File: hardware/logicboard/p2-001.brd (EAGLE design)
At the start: 72 x 72 mm, 53 parts, among them IC1 5V, IC2 4066N, IC3 LTC485N, IC4 74LS07N, J1 LED, J2 PWR, J3 Display, K1 G5V1, Q1 220mA/50V/3.5Ω, Q2 220mA/50V/3.5Ω, T1 2SC1815, U1 DS18B20

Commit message: Pull-down resistor from 100 to 10k.
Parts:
- RN3: value 100 -> 10k
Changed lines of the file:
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@@
 <attribute name="VALUE" x="22" y="36" size="0.8128" layer="27" ratio="10" rot="R90" align="bottom-center"/>
 </element>
-<element name="RN3" library="resistor-net" library_urn="urn:adsk.eagle:library:343" package="RN-5" package3d_urn="urn:adsk.eagle:package:24976/1" value="100" x="24" y="42" smashed="yes" rot="R270">
+<element name="RN3" library="resistor-net" library_urn="urn:adsk.eagle:library:343" package="RN-5" package3d_urn="urn:adsk.eagle:package:24976/1" value="10k" x="24" y="42" smashed="yes" rot="R270">
 <attribute name="MF" value="" x="24" y="42" size="1.778" layer="27" rot="R270" display="off"/>
 <attribute name="MPN" value="" x="24" y="42" size="1.778" layer="27" rot="R270" display="off"/>

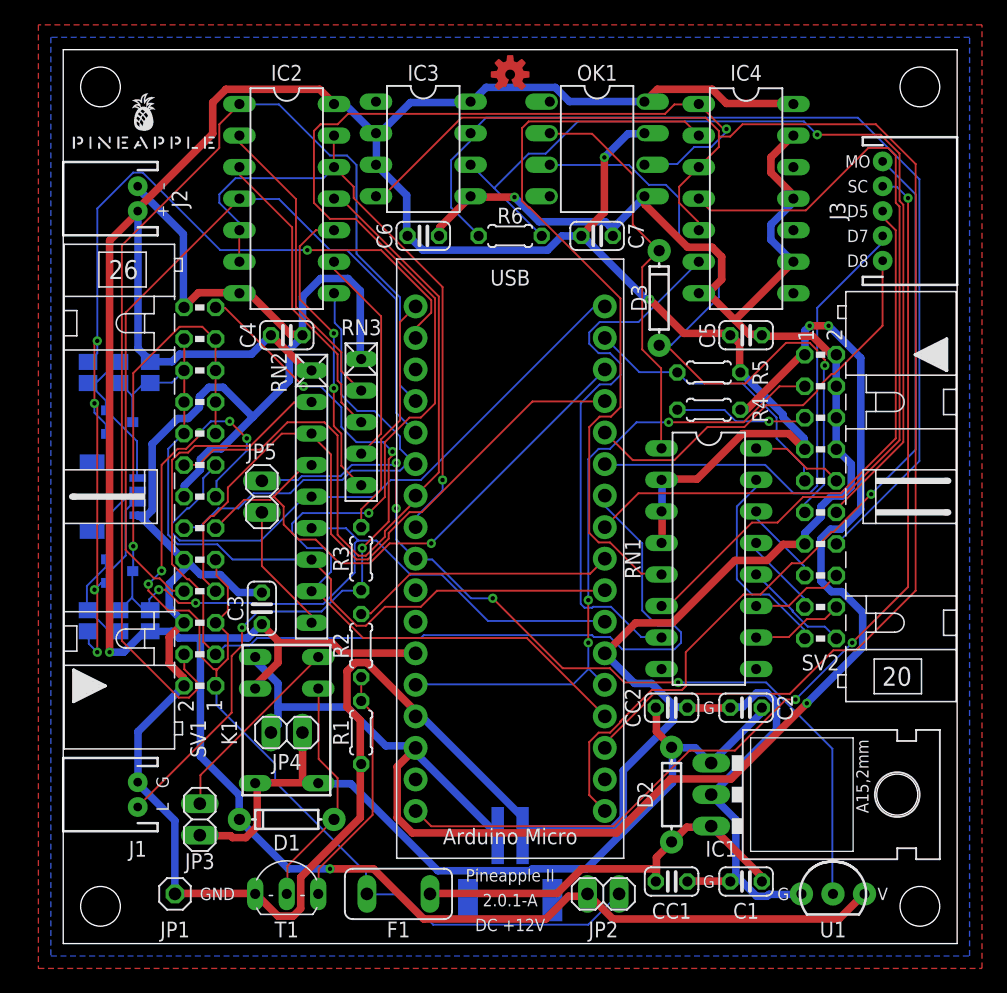
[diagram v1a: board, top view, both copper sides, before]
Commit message: Changed pinout of Display port.
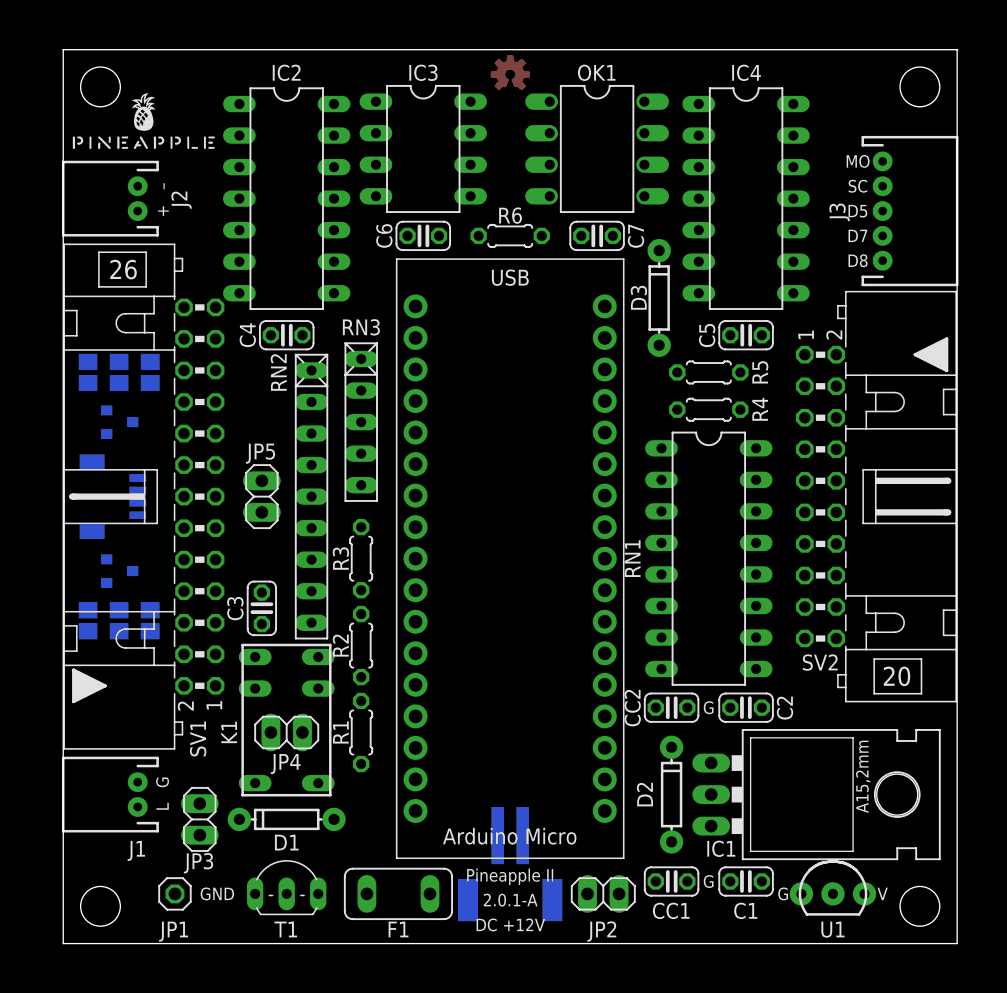
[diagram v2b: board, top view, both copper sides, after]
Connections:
- net DISP1: now also J3.1; no longer J3.3
- net DISP2: now also J3.2; no longer J3.4
- net DISP3: now also J3.3; no longer J3.5
- net MOSI: now also J3.4; no longer J3.1
- net SCLK: now also J3.5; no longer J3.2
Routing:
- net GND: track 338.6 -> 0.00 mm, vias 1 -> 0
- net VCC: track 311.7 -> 0.00 mm, vias 4 -> 0
- net RX: track 124.2 -> 0.00 mm, vias 2 -> 0
- net TX: track 123.2 -> 0.00 mm
- net +12V: track 121.4 -> 0.00 mm, vias 3 -> 0
- net +5V: track 91.2 -> 0.00 mm, vias 5 -> 0
- net ANLG1: track 91.1 -> 0.00 mm
- net VDD: track 87.9 -> 0.00 mm, vias 5 -> 0
- net SDA: track 86.4 -> 0.00 mm, vias 3 -> 0
- net DTCT1: track 84.4 -> 0.00 mm
- net SCLK: track 81.9 -> 0.00 mm, vias 3 -> 0
- net MTX-: track 80.7 -> 0.00 mm
- net MTX+: track 75.3 -> 0.00 mm, vias 1 -> 0
- net THS: track 71.5 -> 0.00 mm, vias 4 -> 0
- net V12V: track 69.7 -> 0.00 mm
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- removed copper zone on layer 1, net GND
- removed copper zone on layer 16, net GND

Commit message: Document update.
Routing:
- net GND: track 0.00 -> 325.6 mm, vias 0 -> 4
- net VCC: track 0.00 -> 306.2 mm, vias 0 -> 3
- net RX: track 0.00 -> 111.5 mm
- net +12V: track 0.00 -> 98.2 mm, vias 0 -> 1
- net LED0A: track 0.00 -> 97.9 mm, vias 0 -> 2
- net TX: track 0.00 -> 90.9 mm, vias 0 -> 2
- net ANLG1: track 0.00 -> 86.0 mm, vias 0 -> 1
- net MTX-: track 0.00 -> 81.7 mm
- net VDD: track 0.00 -> 79.1 mm, vias 0 -> 3
- net SDA: track 0.00 -> 78.2 mm, vias 0 -> 2
- net DTCT1: track 0.00 -> 75.2 mm
- net ANLG2: track 0.00 -> 73.9 mm, vias 0 -> 1
- net SCLK: track 0.00 -> 72.7 mm
- net +5V: track 0.00 -> 72.2 mm, vias 0 -> 1
- net V12V: track 0.00 -> 69.6 mm
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- added copper zone on layer 1, net GND
- added copper zone on layer 16, net GND
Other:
- board text added: "F1"

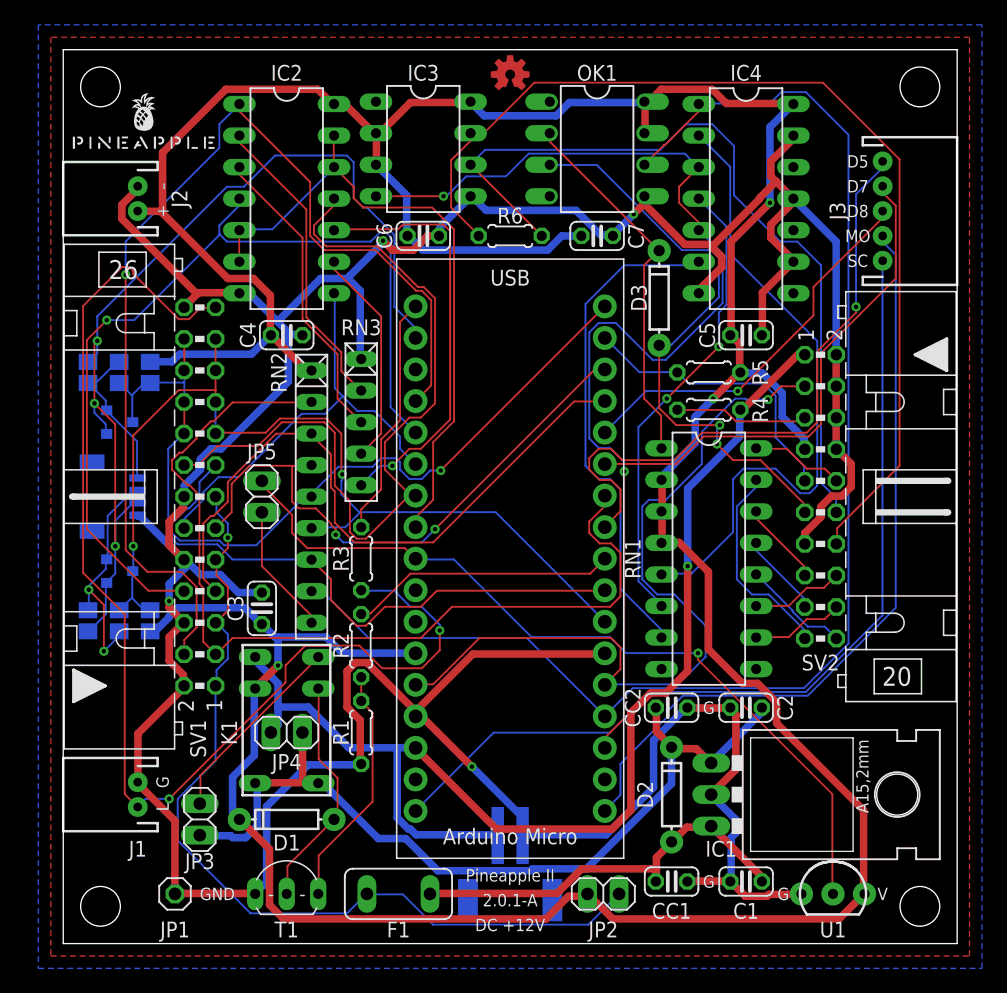
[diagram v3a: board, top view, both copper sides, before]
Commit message: F25 is now connected to AREF.
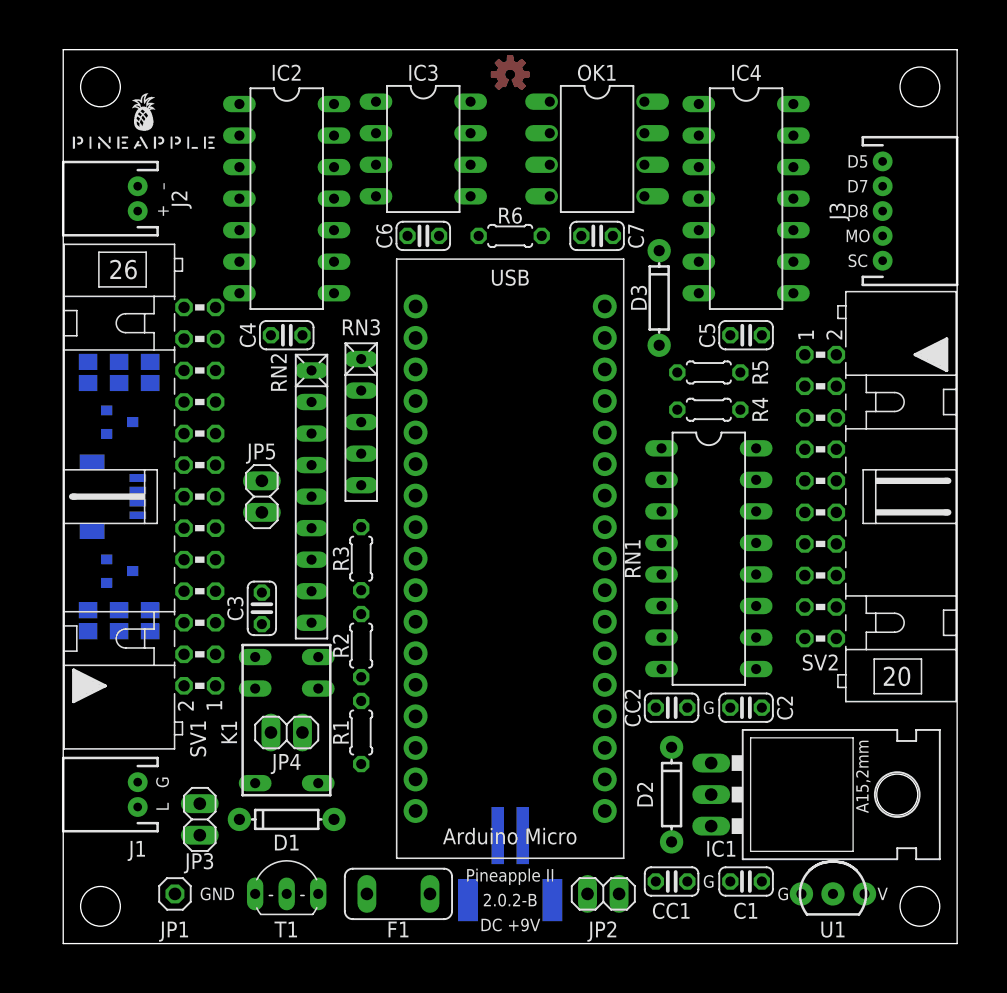
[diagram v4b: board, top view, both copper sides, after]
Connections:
- net AREF: now also SV1.25
- net LED0A: no longer SV1.25
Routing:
- net GND: track 325.6 -> 0.00 mm, vias 4 -> 0
- net VCC: track 306.2 -> 0.00 mm, vias 3 -> 0
- net RX: track 111.5 -> 0.00 mm
- net +12V: track 98.2 -> 0.00 mm, vias 1 -> 0
- net LED0A: track 97.9 -> 0.00 mm, vias 2 -> 0
- net TX: track 90.9 -> 0.00 mm, vias 2 -> 0
- net ANLG1: track 86.0 -> 0.00 mm, vias 1 -> 0
- net MTX-: track 81.7 -> 0.00 mm
- net VDD: track 79.1 -> 0.00 mm, vias 3 -> 0
- net SDA: track 78.2 -> 0.00 mm, vias 2 -> 0
- net DTCT1: track 75.2 -> 0.00 mm
- net ANLG2: track 73.9 -> 0.00 mm, vias 1 -> 0
- net SCLK: track 72.7 -> 0.00 mm
- net +5V: track 72.2 -> 0.00 mm, vias 1 -> 0
- net V12V: track 69.6 -> 0.00 mm
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- removed copper zone on layer 1, net GND
- removed copper zone on layer 16, net GND
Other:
- board text added: "2.0.2-B"
- board text added: "DC +9V"
- board text removed: "2.0.1-A"
- board text removed: "DC +12V"

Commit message: Reflesh.
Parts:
- removed CC1: 10u, resistor:C025-024X044
- removed CC2: 47u, resistor:C025-024X044
- removed IC4: 74LS07N, 74xx-us:DIL14
- removed JP4: RLYJMP, pinhead:1X02
- removed JP5: SNSPUP, pinhead:1X02
- added C10, C9: 100n, rcl:C025-024X044
- added C8: 10n, resistor:C025-024X044
- added J4: Display, SparkFun-Connectors:JST-5-PTH
- added V1: 5V, v-reg:78XXL
- C1, C2, C3, C4: value 0.1u -> 10n
- C5: value 0.1u -> 22u; device resistor:C025-024X044 -> rcl:C025-050X050
- C6: value 0.1u -> 470n; device resistor:C025-024X044 -> rcl:C050-024X044
- C7: value 0.1u -> 1u; device resistor:C025-024X044 -> rcl:C050-024X044
- D2: device SparkFun-DiscreteSemi:DIODE-1N4148 -> diode:DO41-7.6
- IC1: value 5V -> 4066N; device v-reg:78XXL -> 40xx:DIL14
- IC2: value 4066N -> LTC485N; device 40xx:DIL14 -> linear-technology:DIL08
- IC3: value LTC485N -> 74LS07N; device linear-technology:DIL08 -> 74xx-us:DIL14
- J3: value Display -> RLY; device SparkFun-Connectors:JST-5-PTH -> SparkFun-Connectors:JST-2-PTH
- JP2: value REGJMP -> RLYJMP
- JP3: value RLYOUT -> (none); device pinhead:1X02 -> pinhead:1X03
- JV1: value DC12V -> DC9V
- R4: value 1k -> 120
- R6: value 120 -> 1k
- RN1: value 220 -> 4.7k; device resistor-dil:DIL16 -> resistor-net:RN-9
- RN2: value 4.7k -> 10k; device resistor-net:RN-9 -> resistor-net:RN-5
- RN3: value 10k -> 220; device resistor-net:RN-5 -> resistor-dil:DIL16
- moved J3 71.5 mm to (18.0, 6.00), turned to 180 degrees
- moved IC1 62.0 mm to (18.0, 61.0)
- moved C6 57.8 mm to (52.0, 4.00), turned to 180 degrees
- moved C2 47.6 mm to (18.0, 49.0), turned to 0 degrees
- moved C5 46.1 mm to (45.0, 4.00)
- moved C1 43.9 mm to (12.0, 14.0), turned to 90 degrees
- moved C7 39.1 mm to (52.0, 19.0)
- moved C3 32.7 mm to (29.0, 57.0), turned to 0 degrees
- moved RN1 32.4 mm to (20.0, 36.0)
- moved RN3 30.1 mm to (52.0, 31.0)
- moved JP2 28.6 mm to (18.0, 17.0)
- moved JP3 26.5 mm to (16.0, 36.0), turned to 270 degrees
- moved C4 26.2 mm to (43.0, 57.0)
- moved IC3 26.2 mm to (55.0, 61.0)
- moved R4 21.3 mm to (36.0, 57.0), turned to 180 degrees
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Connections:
- removed net +12V: JP4.1, JV1.1, K1.1, MC1.P$20, R4.2, SV2.1
- removed net +5V: F1.1, JP2.2, SV1.1, SV1.13, SV1.5, SV1.9
- removed net THSPUP: JP5.1, RN2.9
- removed net V12V: C2.1, CC2.1, D2.C, IC1.IN, JP3.1, JP4.2, K1.5, K1.6
- new net +3V3: JQ1.2, MC1.P$33, Q1.1, Q2.1, RC2.2, RC4.2
- new net +9V: JP3.2, JV1.1, R5.2, SV2.1
- new net V9A: C7.1, C9.1, D2.C, J3.1, JP2.2, K1.5, K1.6, V1.IN
- new net V9B: JP2.1, JP3.1, K1.1
- net ANLG1: now also IC1.1; no longer IC2.1
- net ANLG1PDN: now also IC1.2, RN2.2; no longer IC2.2, RN3.2
- net ANLG2: now also IC1.4; no longer IC2.4
- net ANLG2PDN: now also IC1.3, RN2.3; no longer IC2.3, RN3.3
- net ANLG3: now also IC1.8; no longer IC2.8
- net ANLG3PDN: now also IC1.9, RN2.4; no longer IC2.9, RN3.4
- net ANLG4: now also IC1.11; no longer IC2.11
- net ANLG4PDN: now also IC1.10, RN2.5; no longer IC2.10, RN3.5
- net AUX: now also R6.1; no longer R5.1
- net DISP1: now also J4.1; no longer J3.1
- net DISP2: now also J4.2; no longer J3.2
- net DISP3: now also J4.3; no longer J3.3
- net DTCT1: now also RN1.2; no longer RN2.2
- net DTCT2: now also RN1.3; no longer RN2.3
- net DTCT3: now also RN1.4; no longer RN2.4
- net DTCT4: now also RN1.5; no longer RN2.5
- net GND: now also C10.2, C8.2, C9.2, IC1.7, IC2.5, IC3.11, IC3.13, IC3.7, IC3.9, RN2.1, V1.GND; no longer CC1.2, CC2.2, IC1.GND, IC2.7, IC3.5, IC4.11, IC4.13, IC4.7, IC4.9, RN3.1
- net MIDIINSND: now also RN3.1; no longer RN1.1
- net MINSND: now also RN3.16; no longer RN1.16
- net MO1: now also IC3.4, RN3.6; no longer IC4.4, RN1.6
- net MO1RTN: now also RN3.11; no longer RN1.11
- net MO1SND: now also RN3.14; no longer RN1.14
- net MO2: now also IC3.6, RN3.7; no longer IC4.6, RN1.7
- net MO2RTN: now also RN3.10; no longer RN1.10
- net MO2SND: now also RN3.13; no longer RN1.13
- net MOSI: now also J4.4; no longer J3.4
- net MTH: now also IC3.2, RN3.5; no longer IC4.2, RN1.5
- net MTHRTN: now also RN3.12; no longer RN1.12
- net MTHSND: now also RN3.15; no longer RN1.15
- net MTX+: now also IC2.6, R4.1; no longer IC3.6, R6.1
- net MTX-: now also IC2.7, R4.2; no longer IC3.7, R6.2
- net PDN: now also IC1.12, IC1.13, IC1.5, IC1.6; no longer IC2.12, IC2.13, IC2.5, IC2.6
- net PWRLED: now also R5.1; no longer R4.1
- net RLYOUT: now also J3.2; no longer JP3.2
- net RX: now also IC3.1, RN1.8; no longer IC4.1, RN2.8
- net SCL: now also RN1.7; no longer RN2.7
- net SCLK: now also J4.5; no longer J3.5
- net SDA: now also RN1.6; no longer RN2.6
- net THS: now also RN1.9; no longer JP5.2
- net TX: now also IC2.4, IC3.3, IC3.5; no longer IC3.4, IC4.3, IC4.5
- net V5V: now also C5.1, C6.1, V1.OUT; no longer C1.1, CC1.1, IC1.OUT
- net VCC: now also C1.1, C10.1, C2.1, C8.1, F1.1, IC1.14, IC2.2, IC2.3, IC2.8, IC3.14, R6.2, RN1.1, RN3.2, RN3.3, RN3.4, SV1.1, SV1.13, SV1.5, SV1.9; no longer C5.1, C6.1, C7.1, IC2.14, IC3.2, IC3.3, IC3.8, IC4.14, JP2.1, R5.2, RN1.2, RN1.3, RN1.4, RN2.1
- net VDD: now also JP3.3, MC1.P$20; no longer JQ1.2, MC1.P$33, Q1.1, Q2.1, RC2.2, RC4.2
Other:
- board text added: "ARD"
- board text added: "Close here"
- board text added: "REG"
- board text removed: "*Bridge JP2 when regulator IC1 is not installed."
- board text removed: "*Bridge JP4 to bypass the relay K1."
- board text removed: "*Bridge JP5 to install 1-Wire thermal sensor at U1."
- board text removed: "+"
- board text removed: "D5"
- board text removed: "D8"
- board text removed: "F1"
- board text removed: "G"
- board text removed: "JP4"
- board text removed: "JP5"
- board text removed: "L"
- board text removed: "MO"
- board text removed: "SC"
- board text removed: "V"
- board text removed: "–"

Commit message: Reflesh.
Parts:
- JP3: value (none) -> PWRSEL
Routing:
- net VCC: track 0.00 -> 347.1 mm, vias 0 -> 6
- net GND: track 0.00 -> 296.9 mm, vias 0 -> 2
- net +9V: track 0.00 -> 115.7 mm, vias 0 -> 7
- net SCL: track 0.00 -> 113.0 mm, vias 0 -> 1
- net TX: track 0.00 -> 99.2 mm, vias 0 -> 2
- net RX: track 0.00 -> 96.1 mm, vias 0 -> 2
- net SCLK: track 0.00 -> 85.4 mm, vias 0 -> 1
- net MTX-: track 0.00 -> 80.3 mm
- net SDA: track 0.00 -> 77.2 mm, vias 0 -> 1
- net V9A: track 0.00 -> 72.0 mm
- net MTH: track 0.00 -> 71.9 mm
- net MTX+: track 0.00 -> 71.6 mm
- net ANLG1: track 0.00 -> 70.3 mm, vias 0 -> 2
- net MO1: track 0.00 -> 68.6 mm
- net ANLG2: track 0.00 -> 67.7 mm, vias 0 -> 1
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- added copper zone on layer 1, net GND
- added copper zone on layer 16, net GND

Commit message: Reflesh...
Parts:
- added C11: 100n, rcl:C025-024X044
- RN1: device resistor-net:RN-9 -> resistor-net:RN-5
- moved R6 28.2 mm to (24.0, 49.0), turned to 90 degrees
- moved RN2 6.00 mm to (24.0, 36.0)
- moved R3 4.47 mm to (22.0, 27.0), turned to 0 degrees
- moved R1 3.00 mm to (24.0, 14.0)
- moved R2 3.00 mm to (24.0, 21.0)
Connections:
- net ANLG4PDN renamed N$2
- net AREF: now also C11.1, R6.1
- net AUX: no longer R6.1
- net DTCT1: no longer RN1.2
- net DTCT2: no longer RN1.3
- net DTCT3: no longer RN1.4
- net DTCT4: no longer RN1.5
- net GND: now also C11.2
- net RX: now also RN1.2; no longer RN1.8
- net SCL: now also RN1.4; no longer RN1.7
- net SDA: now also RN1.3; no longer RN1.6
- net THS: now also RN1.5; no longer RN1.9
- net V5V: now also C7.1, C9.1; no longer C5.1, C6.1
- net V9A: now also C5.1, C6.1; no longer C7.1, C9.1
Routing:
- net VCC: track 347.1 -> 0.00 mm, vias 6 -> 0
- net GND: track 296.9 -> 0.00 mm, vias 2 -> 0
- net +9V: track 115.7 -> 0.00 mm, vias 7 -> 0
- net SCL: track 113.0 -> 0.00 mm, vias 1 -> 0
- net TX: track 99.2 -> 0.00 mm, vias 2 -> 0
- net RX: track 96.1 -> 0.00 mm, vias 2 -> 0
- net SCLK: track 85.4 -> 0.00 mm, vias 1 -> 0
- net MTX-: track 80.3 -> 0.00 mm
- net SDA: track 77.2 -> 0.00 mm, vias 1 -> 0
- net V9A: track 72.0 -> 0.00 mm
- net MTH: track 71.9 -> 0.00 mm
- net MTX+: track 71.6 -> 0.00 mm
- net ANLG1: track 70.3 -> 0.00 mm, vias 2 -> 0
- net MO1: track 68.6 -> 0.00 mm
- net ANLG2: track 67.7 -> 0.00 mm, vias 1 -> 0
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- removed copper zone on layer 1, net GND
- removed copper zone on layer 16, net GND

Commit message: Making...
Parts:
- SV1: device con-ml:ML26L -> con-ml:ML16L
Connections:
- net AREF: no longer SV1.25
- net GND: no longer SV1.26
- net SCL: no longer SV1.18, SV1.20, SV1.22, SV1.24
- net SDA: no longer SV1.17, SV1.19, SV1.21, SV1.23
